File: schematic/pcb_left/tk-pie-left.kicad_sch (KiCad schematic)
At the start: 42 parts, among them IC1 PCA9539PW,118, U2 TPS61027DRCR

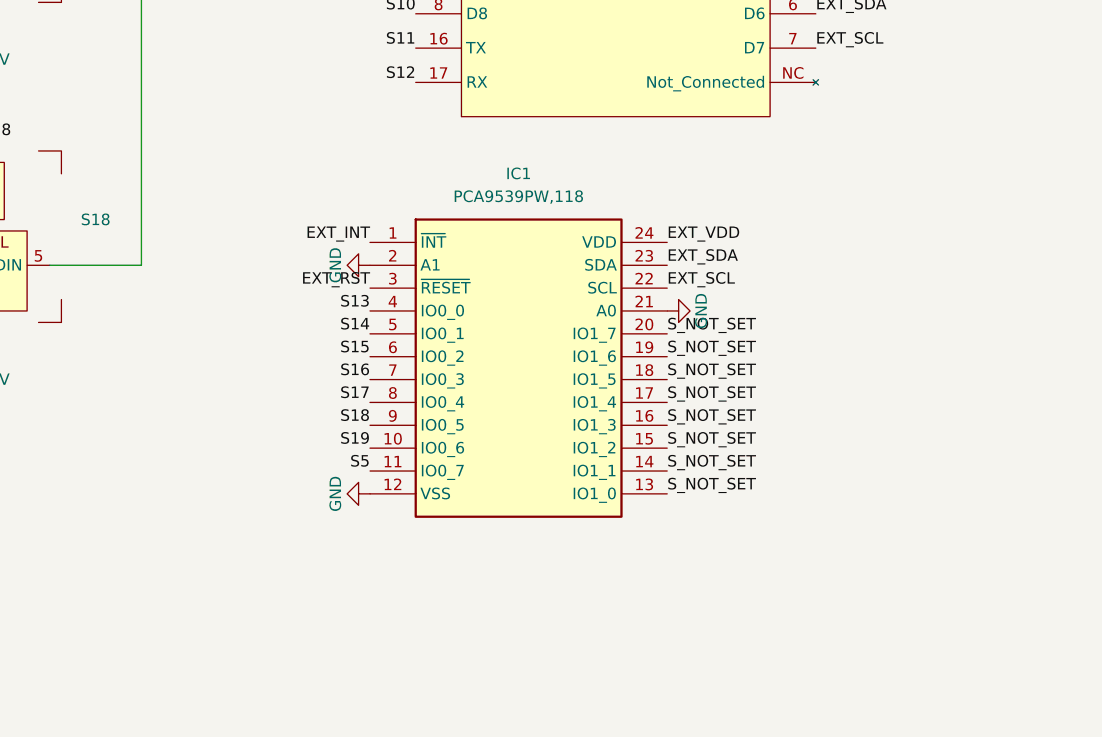
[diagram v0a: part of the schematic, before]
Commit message: Add Nice!View header symbol
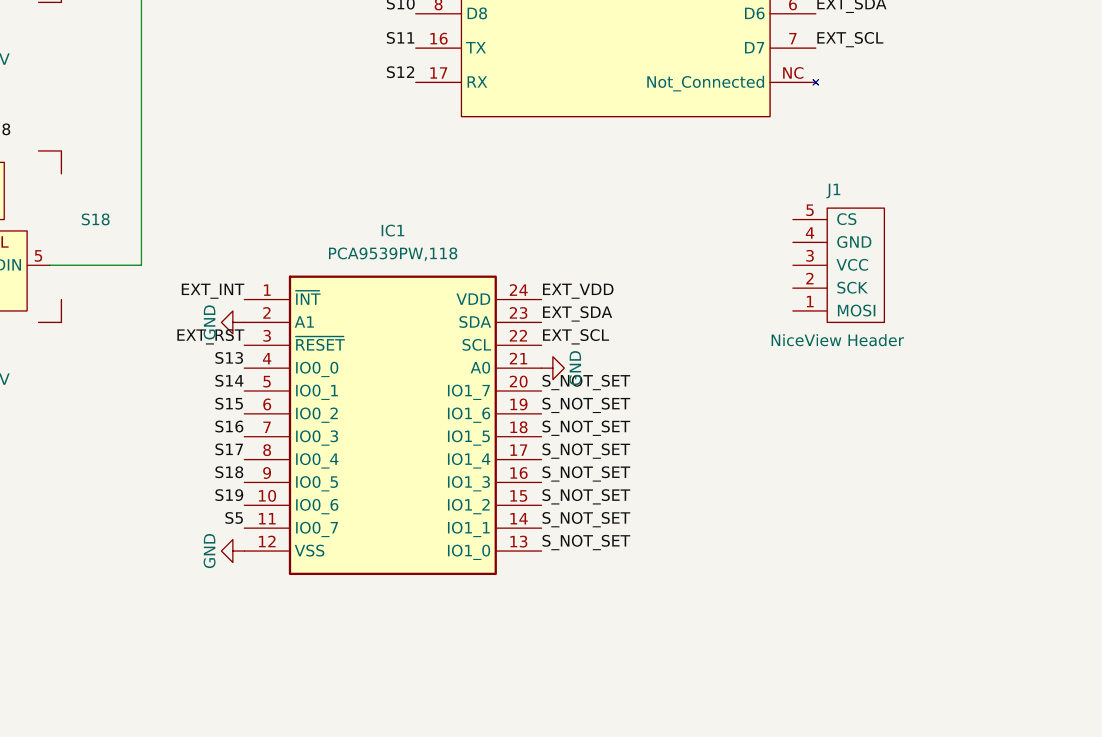
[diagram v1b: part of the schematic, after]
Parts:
- added J1: NiceView Header, Connector_PinHeader_2.54mm:PinHeader_1x05_P2.54mm_Vertical, symbol library:NiceView Header
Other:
- moved on the sheet: IC1
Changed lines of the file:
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@@
 	)
 	(label "S16"
-		(at 214.63 121.92 180)
+		(at 200.66 128.27 180)
 		(fields_autoplaced yes)
 		(effects
@@
 	)
 	(label "S19"
-		(at 214.63 129.54 180)
+		(at 200.66 135.89 180)
 		(fields_autoplaced yes)
 		(effects
@@
 	)
 	(label "EXT_SCL"
-		(at 247.65 111.76 0)
+		(at 233.68 118.11 0)
 		(fields_autoplaced yes)
 		(effects
@@
 	)
 	(label "S_NOT_SET"
-		(at 247.65 119.38 0)
+		(at 233.68 125.73 0)
 		(fields_autoplaced yes)
 		(effects
@@
 	)
 	(label "S14"
-		(at 214.63 116.84 180)
+		(at 200.66 123.19 180)
 		(fields_autoplaced yes)
 		(effects
@@
 	)
 	(label "S13"
-		(at 214.63 114.3 180)
+		(at 200.66 120.65 180)
 		(fields_autoplaced yes)
 		(effects
@@
 	)
 	(label "S_NOT_SET"
-		(at 247.65 129.54 0)
+		(at 233.68 135.89 0)
 		(fields_autoplaced yes)
 		(effects
@@
 	)
 	(label "EXT_INT"
-		(at 214.63 106.68 180)
+		(at 200.66 113.03 180)
 		(fields_autoplaced yes)
 		(effects
@@
 	)
 	(label "EXT_SDA"
-		(at 247.65 109.22 0)
+		(at 233.68 115.57 0)
 		(fields_autoplaced yes)
 		(effects
@@
 	)
 	(label "S15"
-		(at 214.63 119.38 180)
+		(at 200.66 125.73 180)
 		(fields_autoplaced yes)
 		(effects
@@
 	)
 	(label "S_NOT_SET"
-		(at 247.65 116.84 0)
+		(at 233.68 123.19 0)
 		(fields_autoplaced yes)
 		(effects
@@
 	)
 	(label "S_NOT_SET"
-		(at 247.65 127 0)
+		(at 233.68 133.35 0)
 		(fields_autoplaced yes)
 		(effects
@@
 	)
 	(label "S18"
-		(at 214.63 127 180)
+		(at 200.66 133.35 180)
 		(fields_autoplaced yes)
 		(effects
@@
 	)
 	(label "S_NOT_SET"
-		(at 247.65 121.92 0)
+		(at 233.68 128.27 0)
 		(fields_autoplaced yes)
 		(effects
@@
 	)
 	(label "S17"
-		(at 214.63 124.46 180)
+		(at 200.66 130.81 180)
 		(fields_autoplaced yes)
 		(effects
@@
 	)
 	(label "EXT_RST"
-		(at 214.63 111.76 180)
+		(at 200.66 118.11 180)
 		(fields_autoplaced yes)
 		(effects
@@
 	)
 	(label "S5"
-		(at 214.63 132.08 180)
+		(at 200.66 138.43 180)
 		(fields_autoplaced yes)
 		(effects
@@
 	)
 	(label "S_NOT_SET"
-		(at 247.65 134.62 0)
+		(at 233.68 140.97 0)
 		(fields_autoplaced yes)
 		(effects
@@
 	)
 	(label "S_NOT_SET"
-		(at 247.65 132.08 0)
+		(at 233.68 138.43 0)
 		(fields_autoplaced yes)
 		(effects
@@
 	)
 	(label "EXT_VDD"
-		(at 247.65 106.68 0)
+		(at 233.68 113.03 0)
 		(fields_autoplaced yes)
 		(effects
@@
 	)
 	(label "S_NOT_SET"
-		(at 247.65 124.46 0)
+		(at 233.68 130.81 0)
 		(fields_autoplaced yes)
 		(effects
@@
 	(symbol
 		(lib_id "power:GND")
-		(at 214.63 134.62 270)
+		(at 200.66 140.97 270)
 		(unit 1)
 		(exclude_from_sim no)
@@
 		(dnp no)
 		(property "Reference" "#PWR077"
-			(at 208.28 134.62 0)
+			(at 194.31 140.97 0)
 			(effects
 				(font
@@
 		)
 		(property "Value" "GND"
-			(at 210.82 134.62 0)
+			(at 196.85 140.97 0)
 			(effects
 				(font
@@
 		)
 		(property "Footprint" ""
-			(at 214.63 134.62 0)
+			(at 200.66 140.97 0)
 			(effects
 				(font
@@
 		)
 		(property "Datasheet" ""
-			(at 214.63 134.62 0)
+			(at 200.66 140.97 0)
 			(effects
 				(font
@@
 		)
 		(property "Description" ""
-			(at 214.63 134.62 0)
+			(at 200.66 140.97 0)
 			(effects
 				(font
@@
 	(symbol
 		(lib_id "power:GND")
-		(at 214.63 109.22 270)
+		(at 200.66 115.57 270)
 		(unit 1)
 		(exclude_from_sim no)
@@
 		(dnp no)
 		(property "Reference" "#PWR079"
-			(at 208.28 109.22 0)
+			(at 194.31 115.57 0)
 			(effects
 				(font
@@
 		)
 		(property "Value" "GND"
-			(at 210.82 109.22 0)
+			(at 196.85 115.57 0)
 			(effects
 				(font
@@
 		)
 		(property "Footprint" ""
-			(at 214.63 109.22 0)
+			(at 200.66 115.57 0)
 			(effects
 				(font
@@
 		)
 		(property "Datasheet" ""
-			(at 214.63 109.22 0)
+			(at 200.66 115.57 0)
 			(effects
 				(font
@@
 		)
 		(property "Description" ""
-			(at 214.63 109.22 0)
+			(at 200.66 115.57 0)
 			(effects
 				(font
@@
 	(symbol
 		(lib_id "library:PCA9539PW,118")
-		(at 214.63 106.68 0)
+		(at 200.66 113.03 0)
 		(unit 1)
 		(exclude_from_sim no)
@@
 		(fields_autoplaced yes)
 		(property "Reference" "IC1"
-			(at 231.14 99.06 0)
+			(at 217.17 105.41 0)
 			(effects
 				(font
@@
 		)
 		(property "Value" "PCA9539PW,118"
-			(at 231.14 101.6 0)
+			(at 217.17 107.95 0)
 			(effects
 				(font
@@
 		)
 		(property "Footprint" "SOP65P640X110-24N"
-			(at 243.84 201.6 0)
+			(at 229.87 207.95 0)
 			(effects
 				(font
@@
 		)
 		(property "Datasheet" "http://www.nxp.com/docs/en/data-sheet/PCA9539_PCA9539R.pdf"
-			(at 243.84 301.6 0)
+			(at 229.87 307.95 0)
 			(effects
 				(font
@@
 		)
 		(property "Description" "16-bit I2C-bus and SMBus low power I/O port with interrupt and reset"
-			(at 230.886 94.996 0)
+			(at 216.916 101.346 0)
 			(effects
 				(font
@@
 		)
 		(property "Height" "1.1"
-			(at 243.84 501.6 0)
+			(at 229.87 507.95 0)
 			(effects
 				(font
@@
 		)
 		(property "Manufacturer_Name" "NXP"
-			(at 243.84 601.6 0)
+			(at 229.87 607.95 0)
 			(effects
 				(font
@@
 		)
 		(property "Manufacturer_Part_Number" "PCA9539PW,118"
-			(at 243.84 701.6 0)
+			(at 229.87 707.95 0)
 			(effects
 				(font
@@
 		)
 		(property "Mouser Part Number" "771-PCA9539PW-T"
-			(at 243.84 801.6 0)
+			(at 229.87 807.95 0)
 			(effects
 				(font
@@
 		)
 		(property "Mouser Price/Stock" "https://www.mouser.co.uk/ProductDetail/NXP-Semiconductors/PCA9539PW118?qs=LOCUfHb8d9tPW%252BCH%252Bhc6uw%3D%3D"
-			(at 243.84 901.6 0)
+			(at 229.87 907.95 0)
 			(effects
 				(font
@@
 		)
 		(property "Arrow Part Number" "PCA9539PW,118"
-			(at 243.84 1001.6 0)
+			(at 229.87 1007.95 0)
 			(effects
 				(font
@@
 		)
 		(property "Arrow Price/Stock" "https://www.arrow.com/en/products/pca9539pw118/nxp-semiconductors?region=nac"
-			(at 243.84 1101.6 0)
+			(at 229.87 1107.95 0)
 			(effects
 				(font
@@
 	)
 	(symbol
+		(lib_id "library:NiceView Header")
+		(at 265.43 109.22 180)
+		(unit 1)
+		(exclude_from_sim no)
+		(in_bom yes)
+		(on_board yes)
+		(dnp no)
+		(property "Reference" "J1"
+			(at 265.43 100.838 0)
+			(effects
+				(font
+					(size 1.27 1.27)
+				)
+				(justify right)
+			)
+		)
+		(property "Value" "NiceView Header"
+			(at 259.08 117.602 0)
+			(effects
+				(font
+					(size 1.27 1.27)
+				)
+				(justify right)
+			)
+		)
+		(property "Footprint" "Connector_PinHeader_2.54mm:PinHeader_1x05_P2.54mm_Vertical"
+			(at 265.43 122.936 0)
+			(effects
+				(font
+					(size 1.27 1.27)
+				)
+				(hide yes)
+			)
+		)
+		(property "Datasheet" "~"
+			(at 263.652 122.936 0)
+			(effects
+				(font
+					(size 1.27 1.27)
+				)
+				(hide yes)
+			)
+		)
+		(property "Description" "Header for the Nice!View SPI display"
+			(at 264.668 125.73 0)
+			(effects
+				(font
+					(size 1.27 1.27)
+				)
+				(hide yes)
+			)
+		)
+		(pin "1"
+		)
+		(pin "2"
+		)
+		(pin "4"
+		)
+		(pin "5"
+		)
+		(pin "3"
+		)
+		(instances
+			(project ""
+				(path "/9b6bc1bb-4d53-4a7c-b909-4e79c2146edb"
+					(reference "J1")
+					(unit 1)
+				)
+			)
+		)
+	)
+	(symbol
 		(lib_id "power:GND")
 		(at 264.16 46.99 90)
@@
 	(symbol
 		(lib_id "power:GND")
-		(at 247.65 114.3 90)
+		(at 233.68 120.65 90)
 		(unit 1)
 		(exclude_from_sim no)
@@
 		(dnp no)
 		(property "Reference" "#PWR078"
-			(at 254 114.3 0)
+			(at 240.03 120.65 0)
 			(effects
 				(font
@@
 		)
 		(property "Value" "GND"
-			(at 251.46 114.3 0)
+			(at 237.49 120.65 0)
 			(effects
 				(font
@@
 		)
 		(property "Footprint" ""
-			(at 247.65 114.3 0)
+			(at 233.68 120.65 0)
 			(effects
 				(font
@@
 		)
 		(property "Datasheet" ""
-			(at 247.65 114.3 0)
+			(at 233.68 120.65 0)
 			(effects
 				(font
@@
 		)
 		(property "Description" ""
-			(at 247.65 114.3 0)
+			(at 233.68 120.65 0)
 			(effects
 				(font

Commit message: Add footprints for boost circuit
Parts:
- C4, C5: footprint (none) -> Capacitor_SMD:C_1210_3225Metric_Pad1.33x2.70mm_HandSolder
- L2: footprint (none) -> Inductor_SMD:L_Cenker_CKCS5040
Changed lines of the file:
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@@
 			)
 		)
-		(property "Footprint" ""
+		(property "Footprint" "Capacitor_SMD:C_1210_3225Metric_Pad1.33x2.70mm_HandSolder"
 			(at 239.0648 283.21 0)
 			(effects
@@
 			)
 		)
-		(property "Footprint" ""
+		(property "Footprint" "Inductor_SMD:L_Cenker_CKCS5040"
 			(at 287.02 262.89 0)
 			(effects
@@
 			)
 		)
-		(property "Footprint" ""
+		(property "Footprint" "Capacitor_SMD:C_1210_3225Metric_Pad1.33x2.70mm_HandSolder"
 			(at 225.7552 290.83 0)
 			(effects

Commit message: Start wiring up components
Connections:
- net EXT_VDD is gone; now on net +5V: IC1.24 (VDD)
- net LED_CTRL: now also U1.4 (LP_RX); no longer U1.20 (SCL)
- net S1: now also IC1.8 (IO0_4); no longer U1.23 (DAT3)
- net S10: now also IC1.16 (IO1_3); no longer U1.8 (D8)
- net S11: now also U1.9 (D9); no longer U1.16 (TX)
- net S12: now also U1.18 (CMD); no longer U1.17 (RX)
- net S13: now also IC1.6 (IO0_2); no longer IC1.4 (IO0_0)
- net S15: now also IC1.11 (IO0_7); no longer IC1.6 (IO0_2)
- net S16: now also IC1.15 (IO1_2); no longer IC1.7 (IO0_3)
- net S17: now also U1.1 (D1); no longer IC1.8 (IO0_4)
- net S18: now also U1.14 (D14); no longer IC1.9 (IO0_5)
- net S19: now also IC1.4 (IO0_0); no longer IC1.10 (IO0_6)
- net S2: now also IC1.10 (IO0_6); no longer U1.22 (DAT2)
- net S20: now also IC1.20 (IO1_7); no longer U1.3 (D3)
- net S21: now also IC1.19 (IO1_6); no longer U1.2 (D2)
- net S22: now also IC1.18 (IO1_5); no longer U1.15 (D15)
- net S3: now also IC1.13 (IO1_0); no longer U1.21 (DAT1)
- net S4: now also IC1.17 (IO1_4); no longer U1.20 (SCL)
- net S5: no longer IC1.11 (IO0_7)
- net S6: now also U1.20 (SCL); no longer U1.9 (D9)
- net S7: now also IC1.7 (IO0_3); no longer U1.18 (CMD)
- net S8: now also IC1.9 (IO0_5); no longer U1.1 (D1)
- net S9: now also IC1.14 (IO1_1); no longer U1.14 (D14)
- net 5V_EN: now reaches PS1.1 (CE)
- net 5V_EN: now also U1.5 (LP_TX)
- net EXT_INT renamed GPIOE_INT
- net GPIOE_INT: now also U1.15 (D15)
- net EXT_RST renamed GPIOE_RST
- net GPIOE_RST: now also U1.2 (D2)
- net EXT_SCL renamed GPIOE_SCL
- net EXT_SDA renamed GPIOE_SDA
- removed net S_NOT_SET: IC1.13 (IO1_0), IC1.14 (IO1_1), IC1.15 (IO1_2), IC1.16 (IO1_3), IC1.17 (IO1_4), IC1.18 (IO1_5), IC1.19 (IO1_6), IC1.20 (IO1_7), U1.19 (SDA), U1.4 (LP_RX), U1.5 (LP_TX)
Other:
- note added: "LOGIC LEVEL SHIFTER"
- note added: "TODO:"

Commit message: Add logic level shifter to schematic
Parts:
- added U3: SN74LVC1T45DCK, Package_TO_SOT_SMD:SOT-363_SC-70-6_Handsoldering, symbol Logic_LevelTranslator:SN74LVC1T45DCK
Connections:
- net +3.3V: now also U3.6 (VCCB)
- net +5V: now also U3.1 (VCCA)
- net GND: now also U3.2 (GND), U3.5 (DIR)
- net LED_CTRL: now also U3.4 (B)
- net NEOPIXEL_DIN: now also U3.3 (A)
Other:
- note removed: "LOGIC LEVEL SHIFTER"
- note removed: "TODO:"
- moved on the sheet: E1, E2, E3, E4, E5, E6, IC1, J1, U1

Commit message: Add better niceview footprint
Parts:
- J1: value NiceView Header -> NiceView; footprint Connector_PinHeader_2.54mm:PinHeader_1x05_P2.54mm_Vertical -> Footprints:Nice!View Header
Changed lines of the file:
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@@
 			)
 		)
-		(property "Value" "NiceView Header"
-			(at 200.66 107.442 0)
+		(property "Value" "NiceView"
+			(at 202.692 107.188 0)
 			(effects
 				(font
@@
 			)
 		)
-		(property "Footprint" "Connector_PinHeader_2.54mm:PinHeader_1x05_P2.54mm_Vertical"
+		(property "Footprint" "Footprints:Nice!View Header"
 			(at 207.01 112.776 0)
 			(effects

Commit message: More schematics
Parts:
- removed C1, C2: C, symbol Device:C
- removed C3: C_Polarized, symbol Device:C_Polarized_US
- removed L1: L, symbol Device:L
- removed R1, R2, R3, R4, R5: R, symbol Device:R
- removed U2: TPS61027DRCR, DRC0010J, symbol library:TPS61027DRCR
- added J2: Battery Connector, Connector_JST:JST_PH_S2B-PH-SM4-TB_1x02-1MP_P2.00mm_Horizontal, symbol Connector:Conn_01x02_Pin
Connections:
- net +3.3V: now also J1.3 (VCC)
- net GND: now also J1.4 (GND), J2.2 (Pin_2)
- net NV_MOSI: now reaches U1.21 (DAT1)
- net NV_MOSI: now also J1.1 (MOSI)
- net NV_SCK: now reaches U1.22 (DAT2)
- net NV_SCK: now also J1.2 (SCK)
- net  NV_CS: now reaches U1.23 (DAT3)
- net  NV_CS: now also J1.5 (CS)
- net Vbat renamed VBAT
- net VBAT: now also J2.1 (Pin_1)
- no-connect marks 0 -> 3
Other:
- moved on the sheet: J1

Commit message: Move GPIO extender to 3V supply
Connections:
- net +3.3V: now also IC1.24 (VDD)
- net +5V: no longer IC1.24 (VDD)
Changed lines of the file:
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@@
 	)
 	(symbol
-		(lib_id "power:+5V")
-		(at 269.24 128.27 270)
-		(unit 1)
-		(exclude_from_sim no)
-		(in_bom yes)
-		(on_board yes)
-		(dnp no)
-		(fields_autoplaced yes)
-		(property "Reference" "#PWR047"
-			(at 265.43 128.27 0)
-			(effects
-				(font
-					(size 1.27 1.27)
-				)
-				(hide yes)
-			)
-		)
-		(property "Value" "+5V"
-			(at 273.05 128.2699 90)
-			(effects
-				(font
-					(size 1.27 1.27)
-				)
-				(justify left)
-			)
-		)
-		(property "Footprint" ""
-			(at 269.24 128.27 0)
-			(effects
-				(font
-					(size 1.27 1.27)
-				)
-				(hide yes)
-			)
-		)
-		(property "Datasheet" ""
-			(at 269.24 128.27 0)
-			(effects
-				(font
-					(size 1.27 1.27)
-				)
-				(hide yes)
-			)
-		)
-		(property "Description" ""
-			(at 269.24 128.27 0)
-			(effects
-				(font
-					(size 1.27 1.27)
-				)
-				(hide yes)
-			)
-		)
-		(pin "1"
-		)
-		(instances
-			(project "tk-pie-left"
-				(path "/9b6bc1bb-4d53-4a7c-b909-4e79c2146edb"
-					(reference "#PWR047")
-					(unit 1)
-				)
-			)
-		)
-	)
-	(symbol
 		(lib_id "power:GND")
 		(at 91.44 45.72 0)
@@
 					(unit 1)
 				)
+			)
+		)
+	)
+	(symbol
+		(lib_id "power:+3.3V")
+		(at 269.24 128.27 270)
+		(unit 1)
+		(exclude_from_sim no)
+		(in_bom yes)
+		(on_board yes)
+		(dnp no)
+		(property "Reference" "#PWR065"
+			(at 265.43 128.27 0)
+			(effects
+				(font
+					(size 1.27 1.27)
+				)
+				(hide yes)
+			)
+		)
+		(property "Value" "+3.3V"
+			(at 273.05 128.2701 90)
+			(effects
+				(font
+					(size 1.27 1.27)
+				)
+				(justify left)
+			)
+		)
+		(property "Footprint" ""
+			(at 269.24 128.27 0)
+			(effects
+				(font
+					(size 1.27 1.27)
+				)
+				(hide yes)
+			)
+		)
+		(property "Datasheet" ""
+			(at 269.24 128.27 0)
+			(effects
+				(font
+					(size 1.27 1.27)
+				)
+				(hide yes)
+			)
+		)
+		(property "Description" "Power symbol creates a global label with name \"+3.3V\""
+			(at 269.24 128.27 0)
+			(effects
+				(font
+					(size 1.27 1.27)
+				)
+				(hide yes)
+			)
+		)
+		(pin "1"
+		)
+		(instances
+			(project "tk-pie-left"
+				(path "/9b6bc1bb-4d53-4a7c-b909-4e79c2146edb"
+					(reference "#PWR065")
+					(unit 1)
+				)
